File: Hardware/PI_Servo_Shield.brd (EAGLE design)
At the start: 65 x 30 mm, 112 parts, among them J1 RASPBERRYPI-40-PIN-GPIO, J19 QWIIC, J20 USB C, J21 Serial, Q1 2N7002PW, Q4 2N7002PW, U1 PCA9685, U3 CH340C

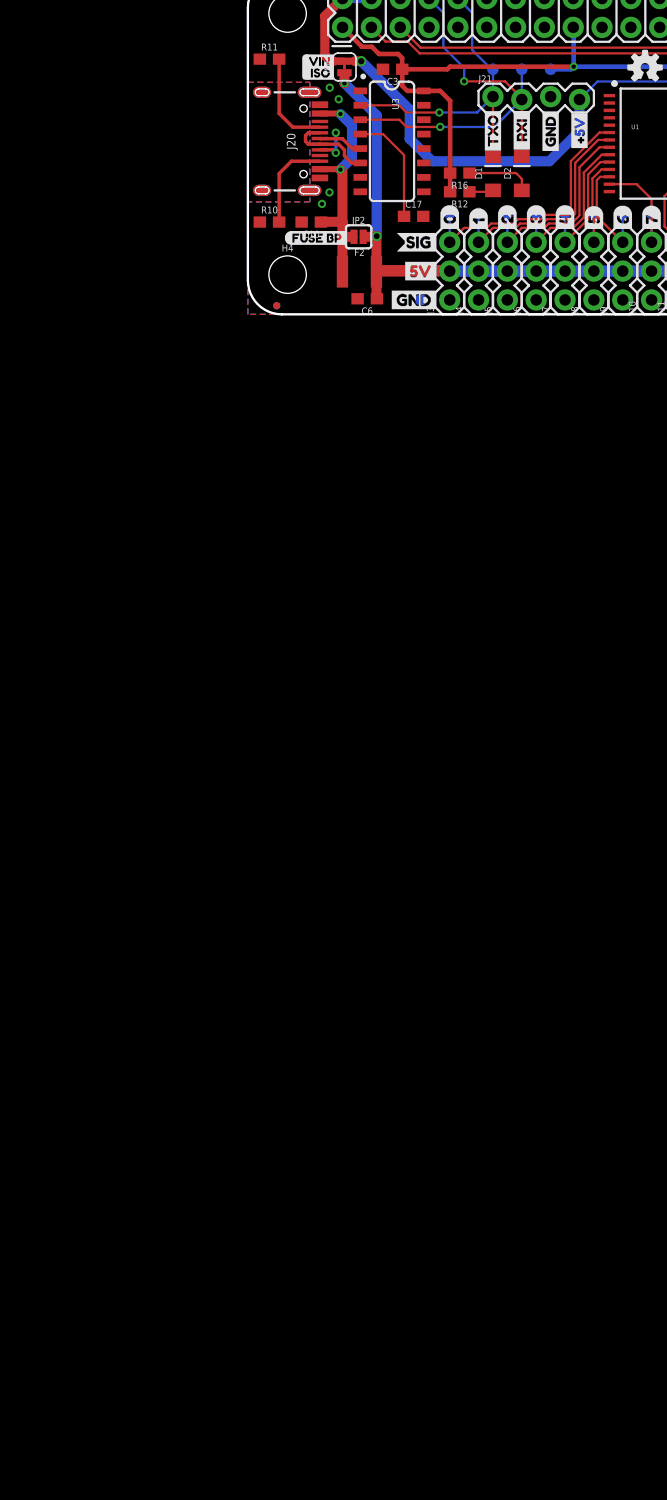
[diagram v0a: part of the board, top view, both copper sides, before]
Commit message: Reverse current blocking diodes and more
-Added reverse current blocking circuits.
-Added auto switching isolation fet between Pi 5V rail and servo rail.
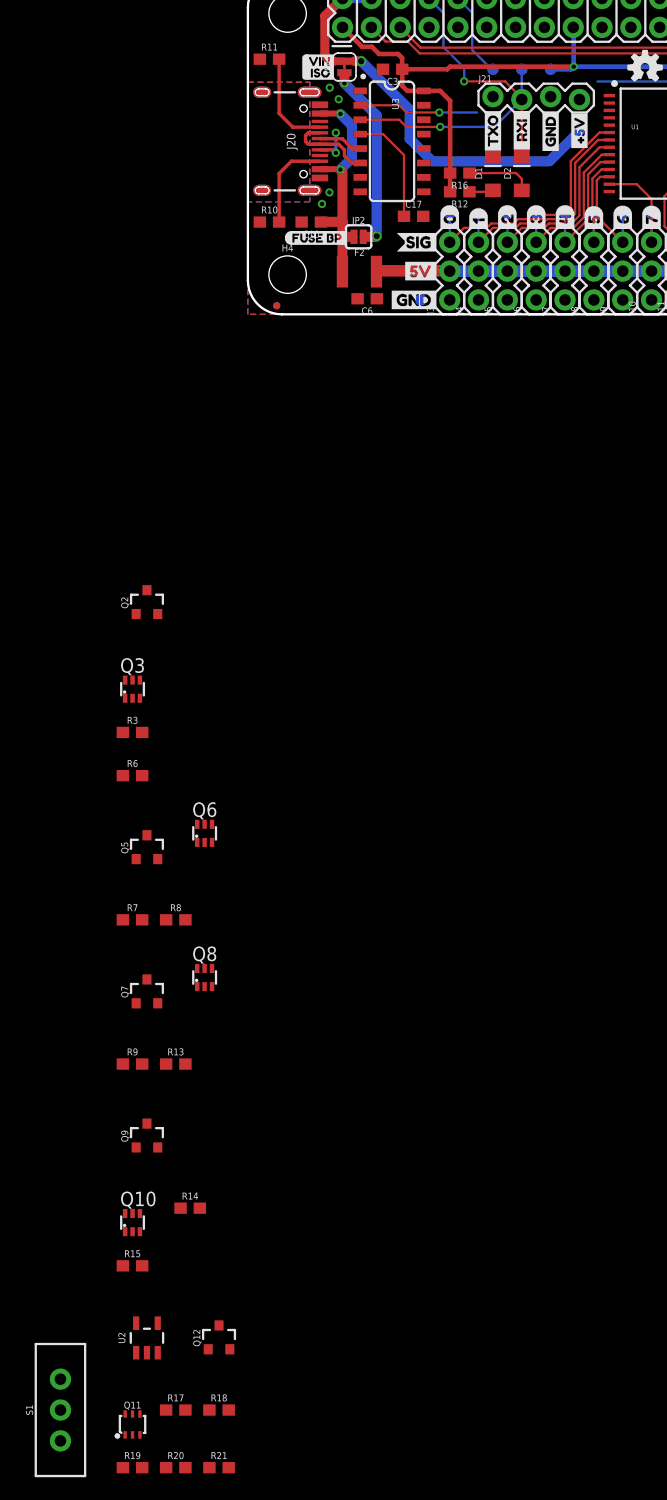
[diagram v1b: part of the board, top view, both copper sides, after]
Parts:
- removed FRAME1: FRAME-LETTER, SparkFun-Aesthetics:CREATIVE_COMMONS
- added FRAME2: FRAME-LEDGER, SparkFun-Aesthetics:CREATIVE_COMMONS
- added Q10, Q3, Q6, Q8: (no value), SparkFun-DiscreteSemi:SOT363_PHILIPS
- added Q11: (no value), SparkFun-DiscreteSemi:SC70-6
- added Q12, Q2, Q5, Q7, Q9: 2.5A/30V/105mΩ, SparkFun-DiscreteSemi:SOT23-3
- added R13, R15, R19, R20, R21, R6, R8: 10k, SparkFun-Resistors:0603
- added R14, R3, R7, R9: 47k, SparkFun-Resistors:0603
- added R17, R18: 100, SparkFun-Resistors:0603
- added S1: (no value), SparkFun-Switches:SWITCH_SPDT_PTH_11.6X4.0MM_LOCK
- added U2: SN74LVC1G32DCKR, SparkFun-IC-Logic:SOT23-5
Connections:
- net RXI renamed PI-TXO
- removed net 5V: C4.1, C8.1, J1.2, J1.4, J21.4, JP4.2, R1.2, R2.2, U1.28
- removed net TXO: D1.C, J1.10, J21.1, TP21.P$1, U3.2
- removed net VIN: C5.+, C6.1, F2.2, J10.2, J11.2, J12.2, J13.2, J14.2, J15.2, J16.2, J17.2, J18.2, J3.2, J4.2, J5.2, J6.2, J7.2, J8.2, J9.2, JP2.2, JP4.1, TP16.P$1
- new net CH340-TXO: D1.C, S1.3, U3.2
- new net N$1: Q5.1, Q6.3, R7.2
- new net N$10: Q3.2, Q3.5, Q3.6, R6.2
- new net N$11: Q6.2, Q6.5, Q6.6, R8.2
- new net N$12: Q11.5, Q11.6, R18.1
- new net N$13: Q11.3, Q12.1, R19.1
- new net N$15: Q7.1, Q8.3, R9.2
- new net N$16: Q8.2, Q8.5, Q8.6, R13.2
- new net N$17: R17.1, U2.4
- new net N$18: Q10.3, Q9.1, R14.2
- new net N$19: Q10.2, Q10.5, Q10.6, R15.2
- new net N$8: Q11.2, R17.2
- new net N$9: Q2.1, Q3.3, R3.2
- new net PI-5V: C4.1, C8.1, J1.2, J1.4, JP4.2, Q10.4, Q12.3, Q7.2, Q8.4, Q9.2, R1.2, R18.2, R19.2, R2.2, U1.28
- new net PI-RXI: J1.10, S1.2, TP21.P$1
- new net RVR-5V: J21.4, Q2.3, Q3.1, Q7.3, Q8.1, R20.2, U2.1
- new net RVR-TXO: J21.1, S1.1
- new net SERVO: C5.+, C6.1, J10.2, J11.2, J12.2, J13.2, J14.2, J15.2, J16.2, J17.2, J18.2, J3.2, J4.2, J5.2, J6.2, J7.2, J8.2, J9.2, JP4.1, Q12.2, Q2.2, Q3.4, Q5.2, Q6.4, TP16.P$1
- new net USB-5V: F2.2, JP2.2, Q10.1, Q5.3, Q6.1, Q9.3, R21.2, U2.2
- net GND: now also Q11.1, Q11.4, R13.1, R14.1, R15.1, R20.1, R21.1, R3.1, R6.1, R7.1, R8.1, R9.1
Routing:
- net VIN: track 78.0 -> 0.00 mm, vias 2 -> 0
- net SERVO: track 0.00 -> 72.3 mm, vias 0 -> 2
- net 5V: track 70.8 -> 0.00 mm, vias 3 -> 0
- net PI-5V: track 0.00 -> 65.8 mm, vias 0 -> 3
- net TXO: track 27.8 -> 0.00 mm, vias 1 -> 0
- net CH340-TXO: track 0.00 -> 10.6 mm, vias 0 -> 1
- net PI-RXI: track 0.00 -> 7.58 mm

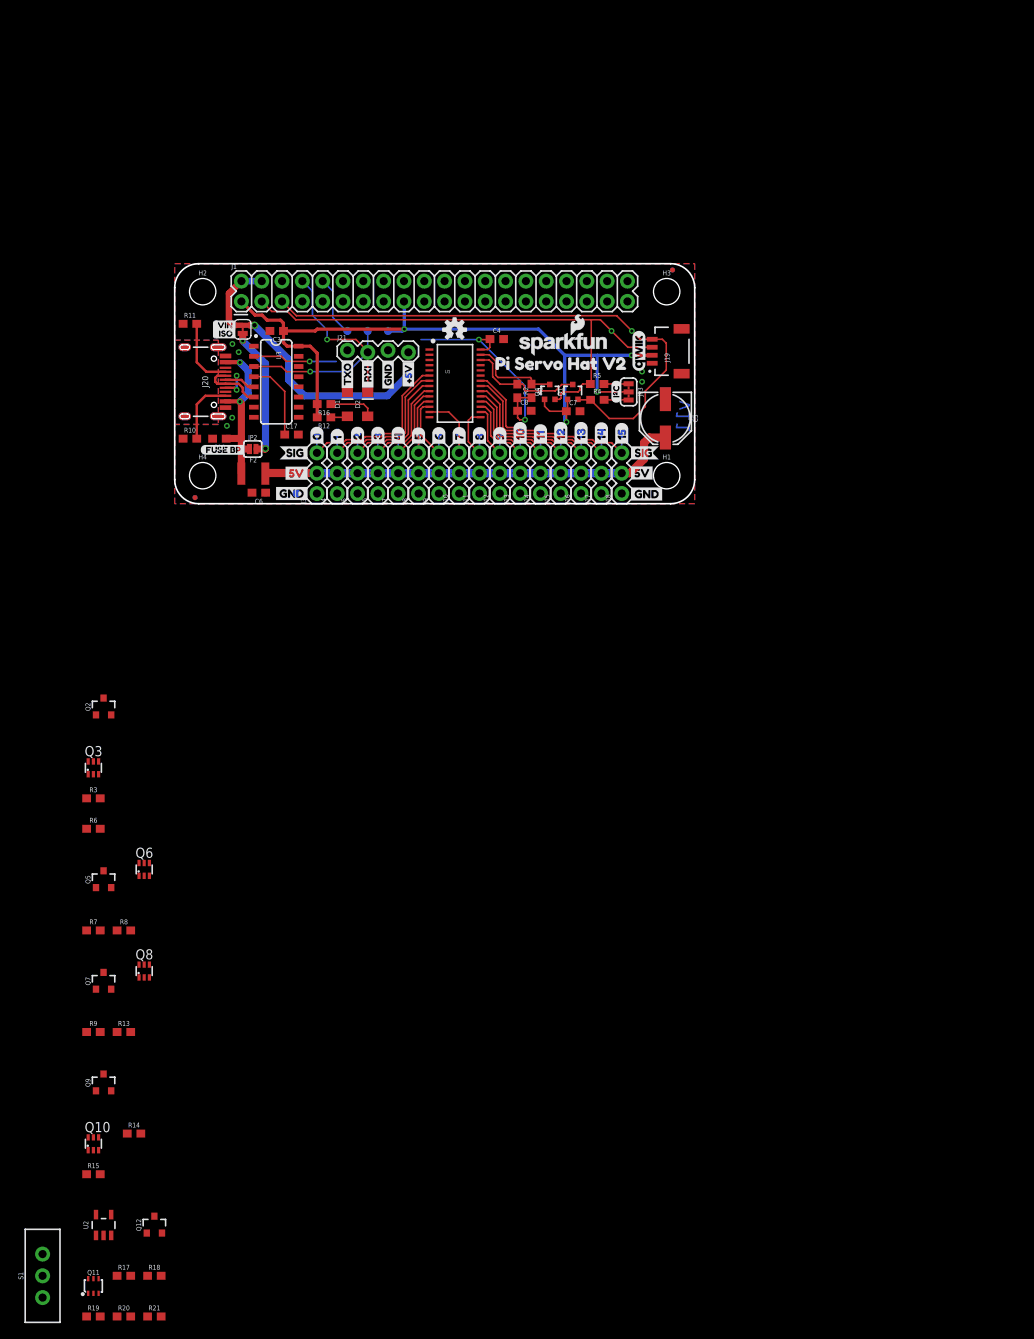
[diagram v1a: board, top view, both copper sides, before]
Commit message: schematic cleanup and some part positioning
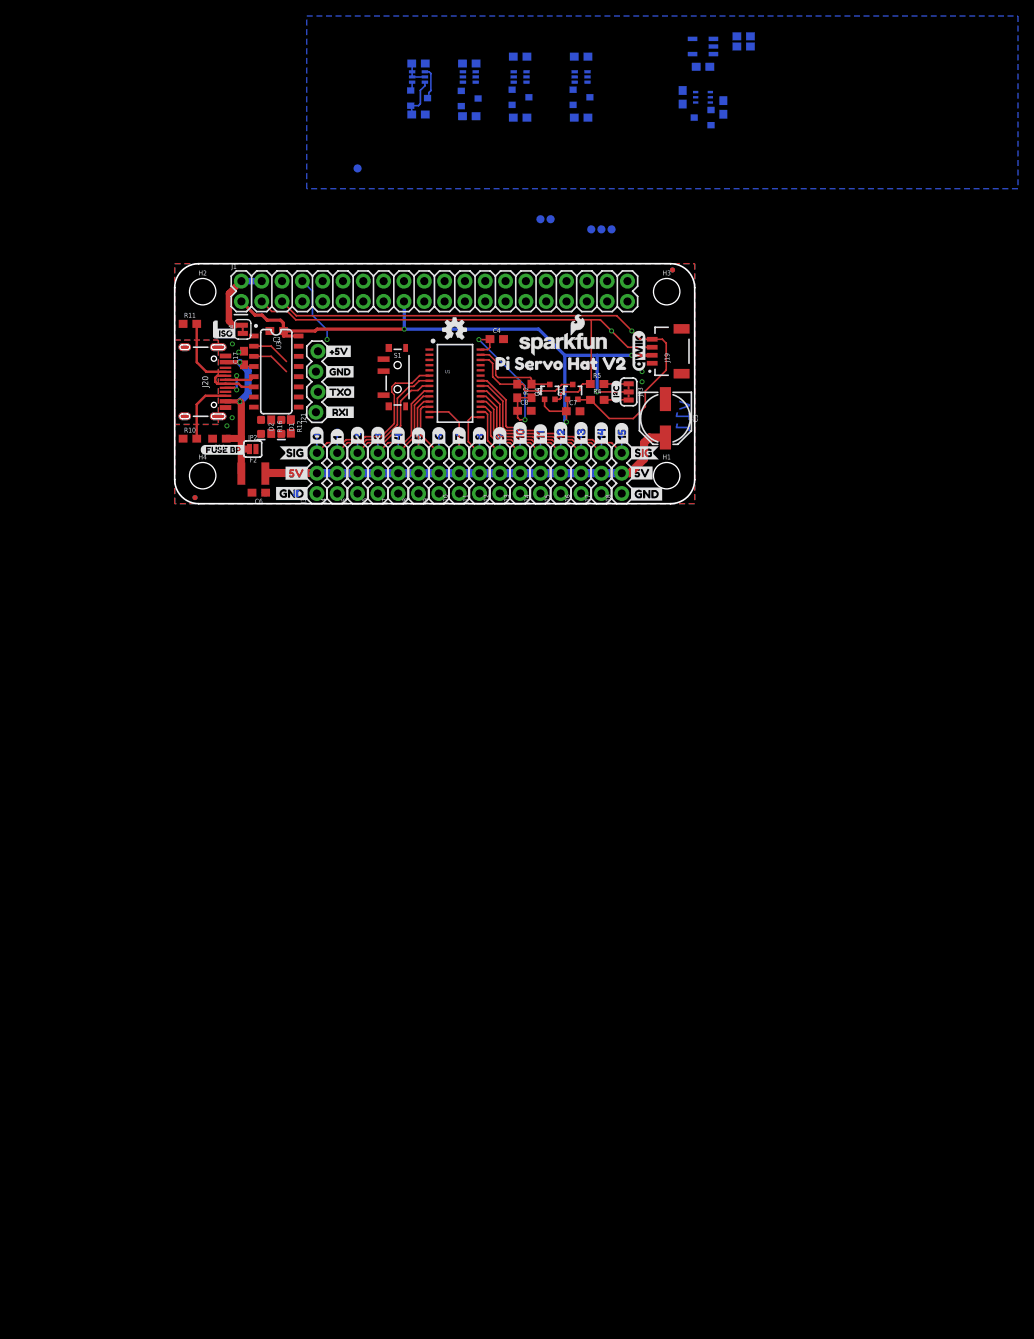
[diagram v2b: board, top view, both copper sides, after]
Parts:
- removed U$31: (no value), buzzard_labels (3):VIN0
- added TP23, TP24, TP25: (no value), SparkFun-Connectors:PAD.03X.04
- D1: device SparkFun-LED:LED-1206-HIDDENSILK -> SparkFun-LED:LED-0603
- D2: value YELLOW -> Yellow; device SparkFun-LED:LED-1206-HIDDENSILK -> SparkFun-LED:LED-0603
- JP4: value VIN ISO -> PI ISO
- S1: device SparkFun-Switches:SWITCH_SPDT_PTH_11.6X4.0MM_LOCK -> SparkFun-Switches:SWITCH_SPST_SMD_A
- moved R20 177.8 mm to (71.1, 58.4), flipped to the bottom
- moved R21 175.0 mm to (71.1, 57.1), flipped to the bottom
- moved R19 170.4 mm to (68.6, 49.5), flipped to the bottom, turned to 270 degrees
- moved R17 167.6 mm to (66.0, 54.6), flipped to the bottom, turned to 180 degrees
- moved Q11 167.0 mm to (66.0, 50.8), flipped to the bottom, turned to 270 degrees
- moved U2 165.3 mm to (66.0, 57.1), flipped to the bottom, turned to 270 degrees
- moved R18 161.4 mm to (63.5, 50.8), flipped to the bottom, turned to 270 degrees
- moved Q12 154.5 mm to (66.0, 48.3), flipped to the bottom, turned to 270 degrees
- moved R15 152.4 mm to (50.8, 55.9), flipped to the bottom
- moved Q10 146.6 mm to (50.8, 53.3), flipped to the bottom, turned to 270 degrees
- moved R14 138.8 mm to (50.8, 48.3), flipped to the bottom
- moved Q9 136.9 mm to (50.8, 50.8), flipped to the bottom, turned to 90 degrees
- moved R13 131.6 mm to (43.2, 55.9), flipped to the bottom
- moved R9 126.1 mm to (43.2, 48.3), flipped to the bottom
- moved Q7 122.1 mm to (43.2, 50.8), flipped to the bottom, turned to 90 degrees
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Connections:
- new net N$20: JP4.1, Q12.3, R18.2, R19.2
- new net VIN: JP4.2
- net CH340-TXO: now also TP23.P$1
- net PI-5V: now also TP24.P$1; no longer JP4.2, Q12.3, R18.2, R19.2
- net PI-RXI: no longer TP21.P$1
- net RVR-5V: now also TP25.P$1
- net RVR-TXO: now also TP21.P$1
- net SERVO: no longer JP4.1
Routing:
- net PI-5V: track 65.8 -> 30.7 mm, vias 3 -> 2
- net PI-TXO: track 37.6 -> 13.4 mm, vias 2 -> 1
- net SERVO: track 72.3 -> 56.8 mm, vias 2 -> 0
- net 3.3V: track 98.4 -> 84.6 mm
- net N$14: track 10.0 -> 1.33 mm
- net PI-RXI: track 7.58 -> 0.00 mm
- net CH340-TXO: track 10.6 -> 4.86 mm, vias 1 -> 0
- net N$6: track 5.84 -> 0.39 mm
- net N$9: track 0.00 -> 5.40 mm
- net RVR-5V: track 0.00 -> 4.09 mm
- net N$10: track 0.00 -> 3.33 mm
- net N$7: track 2.12 -> 0.00 mm
- net D-: track 7.79 -> 6.96 mm
- net CH1: track 20.4 -> 19.7 mm
- net CH2: track 17.5 -> 16.8 mm
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
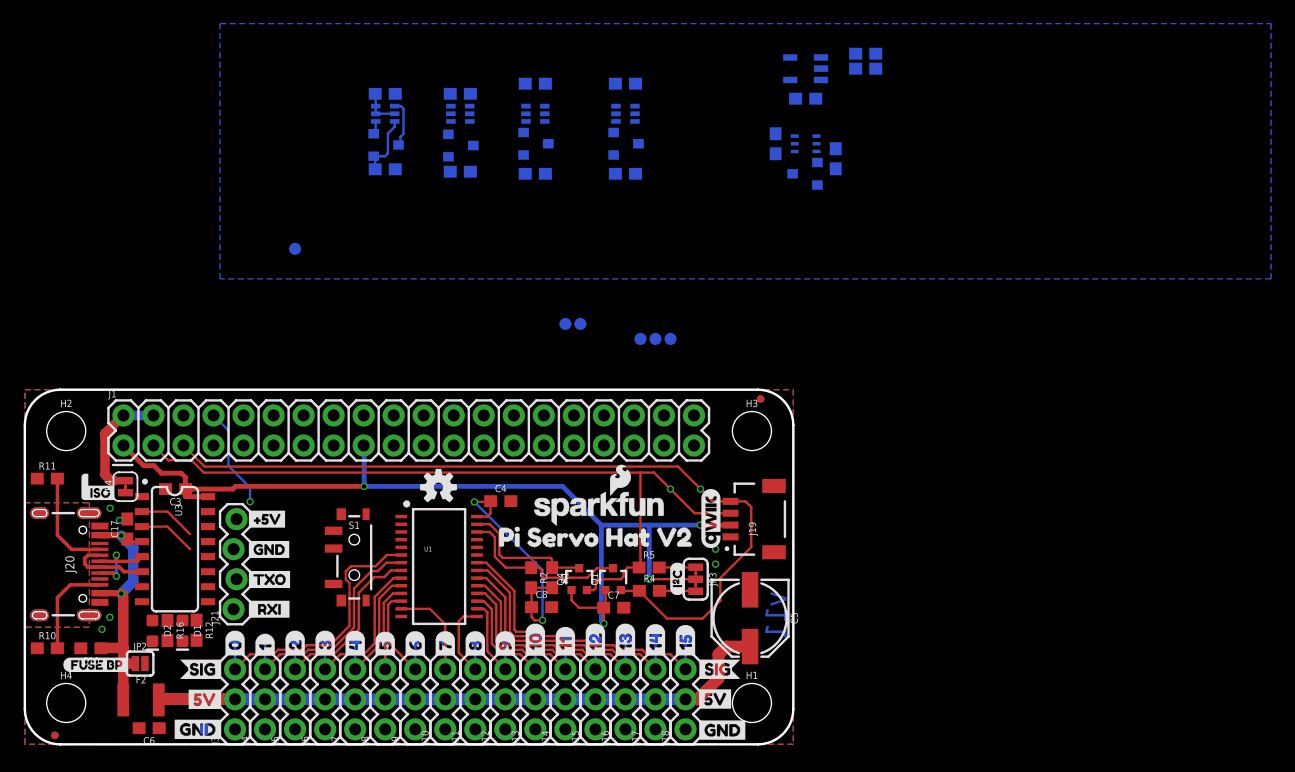
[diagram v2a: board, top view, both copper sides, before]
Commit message: Placed all ideal diodes and routed most things
still need a cap and test points placed and routed.
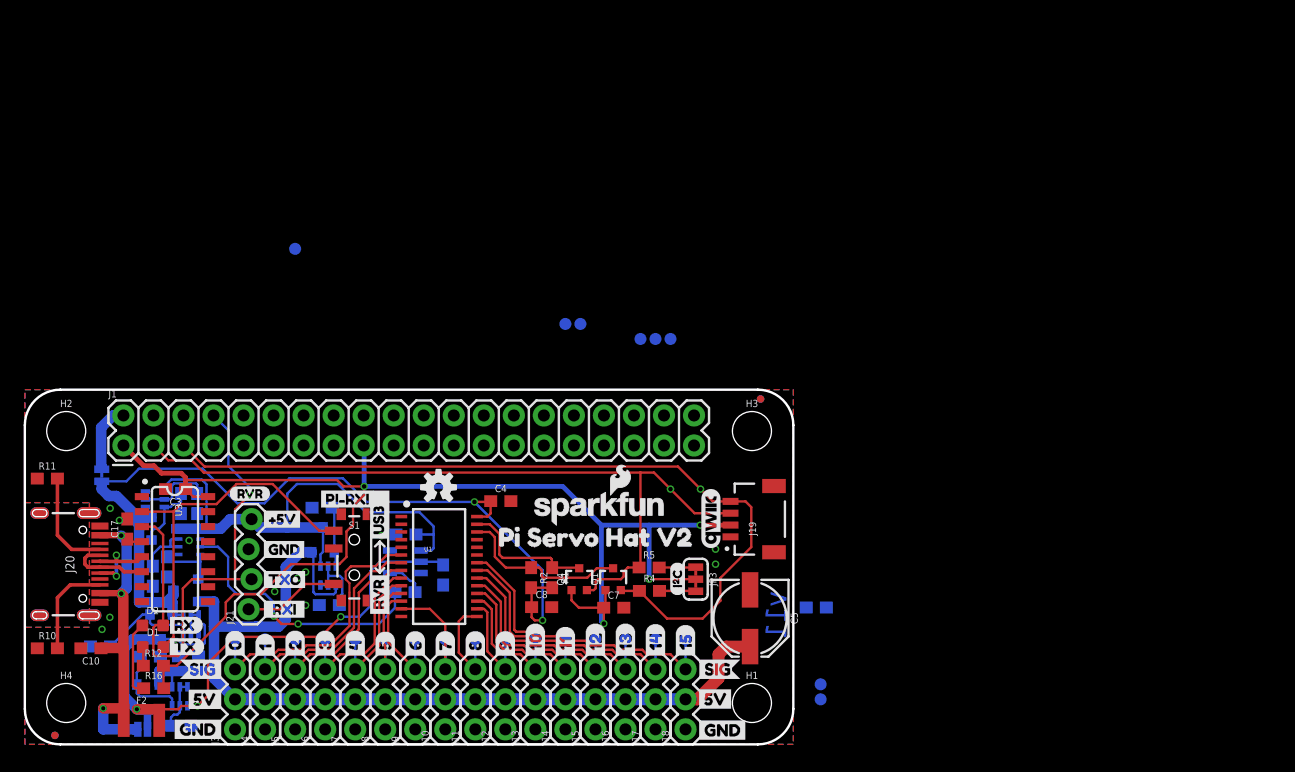
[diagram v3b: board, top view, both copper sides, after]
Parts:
- added U$26: (no value), buzzard_labels (1):PI#RXI2
- added U$31: (no value), buzzard_labels (1):RVR1
- added U$34: (no value), buzzard_labels (1):USB0
- added U$35: (no value), buzzard_labels (3):PI0
- added U$36: (no value), buzzard_labels (2):RX0
- added U$37: (no value), buzzard_labels (2):TX1
- added U$38: (no value), buzzard_labels (4):RVR0
- moved R19 66.3 mm to (12.0, 15.0)
- moved R18 64.1 mm to (10.8, 14.2)
- moved Q12 63.1 mm to (13.7, 13.0)
- moved Q11 62.3 mm to (13.9, 16.7)
- moved R15 60.9 mm to (13.8, 7.44), turned to 180 degrees
- moved R14 59.7 mm to (6.40, 8.28), turned to 180 degrees
- moved R8 58.4 mm to (13.2, 1.57)
- moved C6 57.3 mm to (66.9, 11.6), flipped to the bottom
- moved Q10 56.7 mm to (14.0, 10.2), turned to 0 degrees
- moved Q9 56.6 mm to (11.5, 9.98), turned to 180 degrees
- moved R20 56.3 mm to (32.2, 17.8), turned to 180 degrees
- moved R21 55.8 mm to (35.4, 14.3), turned to 90 degrees
- moved Q6 54.7 mm to (13.1, 4.06), turned to 0 degrees
- moved R17 53.8 mm to (32.2, 12.9), turned to 0 degrees
- moved U2 53.7 mm to (32.2, 15.4)
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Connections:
- removed net VIN: JP4.2
- new net 5V: J1.4
- net CH340-TXO: now also S1.1; no longer S1.3
- net N$20: now also J1.2, JP4.2; no longer JP4.1, Q12.3, R18.2, R19.2
- net PI-5V: now also JP4.1, Q12.3, R18.2, R19.2; no longer J1.2, J1.4
- net RVR-TXO: now also S1.3; no longer S1.1
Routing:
- net USB-5V: track 0.00 -> 53.1 mm, vias 0 -> 3
- net PI-5V: track 30.7 -> 79.3 mm
- net RVR-5V: track 4.09 -> 46.1 mm
- net PI-TXO: track 13.4 -> 42.8 mm
- net 3.3V: track 84.6 -> 112.9 mm
- net SERVO: track 56.8 -> 83.6 mm
- net CH340-TXO: track 4.86 -> 30.7 mm
- net N$8: track 0.00 -> 23.2 mm, vias 0 -> 2
- net N$18: track 0.00 -> 9.04 mm
- net RVR-TXO: track 0.00 -> 8.08 mm
- net N$1: track 0.00 -> 7.19 mm
- net N$16: track 0.00 -> 6.99 mm
- net VBUS: track 21.4 -> 28.1 mm, vias 2 -> 3
- net N$19: track 0.00 -> 6.30 mm
- net N$6: track 0.39 -> 6.44 mm
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
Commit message: V12 routed
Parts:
- removed U$30: (no value), buzzard_labels (5):FUSE_BP5
- added U$39: (no value), buzzard_labels (5):FUSE_BP0
- moved C6 52.6 mm to (14.7, 5.19), turned to 270 degrees
- moved TP21 36.4 mm to (21.6, 16.5), turned to 180 degrees
- moved TP20 35.4 mm to (21.6, 21.6), turned to 180 degrees
- moved TP23 21.3 mm to (16.5, 21.6)
- moved TP25 19.9 mm to (38.1, 17.8)
- moved TP24 16.7 mm to (43.2, 19.1)
- moved TP22 12.7 mm to (52.1, 21.6)
- moved TP16 9.67 mm to (58.4, 8.89)
- moved TP17 8.13 mm to (61.0, 8.89)
- moved C10 1.80 mm to (7.39, 8.10)
- moved C17 1.66 mm to (8.48, 19.9)
- moved R9 1.27 mm to (14.4, 19.8), turned to 0 degrees
- moved R13 0.92 mm to (14.4, 21.3), turned to 0 degrees
- moved R8 0.64 mm to (13.1, 2.21)
- moved F2 0.51 mm to (9.89, 2.54)
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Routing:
- net PI-RXI: track 0.00 -> 19.0 mm, vias 0 -> 1
- net 3.3V: track 112.9 -> 121.0 mm, vias 4 -> 6
- net SERVO: track 83.6 -> 90.4 mm
- net RVR-TXO: track 8.08 -> 12.5 mm, vias 0 -> 1
- net VBUS: track 28.1 -> 24.0 mm
- net PI-5V: track 79.3 -> 82.5 mm
- net N$16: track 6.99 -> 4.17 mm
- net PI-TXO: track 42.8 -> 45.1 mm
- net CH5: track 10.0 -> 12.2 mm, vias 0 -> 1
- net LV_SCL: track 69.2 -> 67.4 mm
- net N$14: track 1.33 -> 2.94 mm
- net RVR-5V: track 46.1 -> 47.4 mm
- net N$4: track 11.6 -> 10.6 mm
- net CH340-TXO: track 30.7 -> 31.7 mm, vias 0 -> 1
- net CH7: track 10.6 -> 9.64 mm
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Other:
- board text added: "v12"
- board text removed: "v11"
